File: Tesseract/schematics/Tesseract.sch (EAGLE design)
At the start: 108 parts, among them IC1 MC7805CDTG, IC2 QUAD_OPAMPD, IC3 NE5532D, IC4 LM4040B10, IC5 NE5532D, Q1 SI2309CDS, Q2 BSS123, Q901 BC846

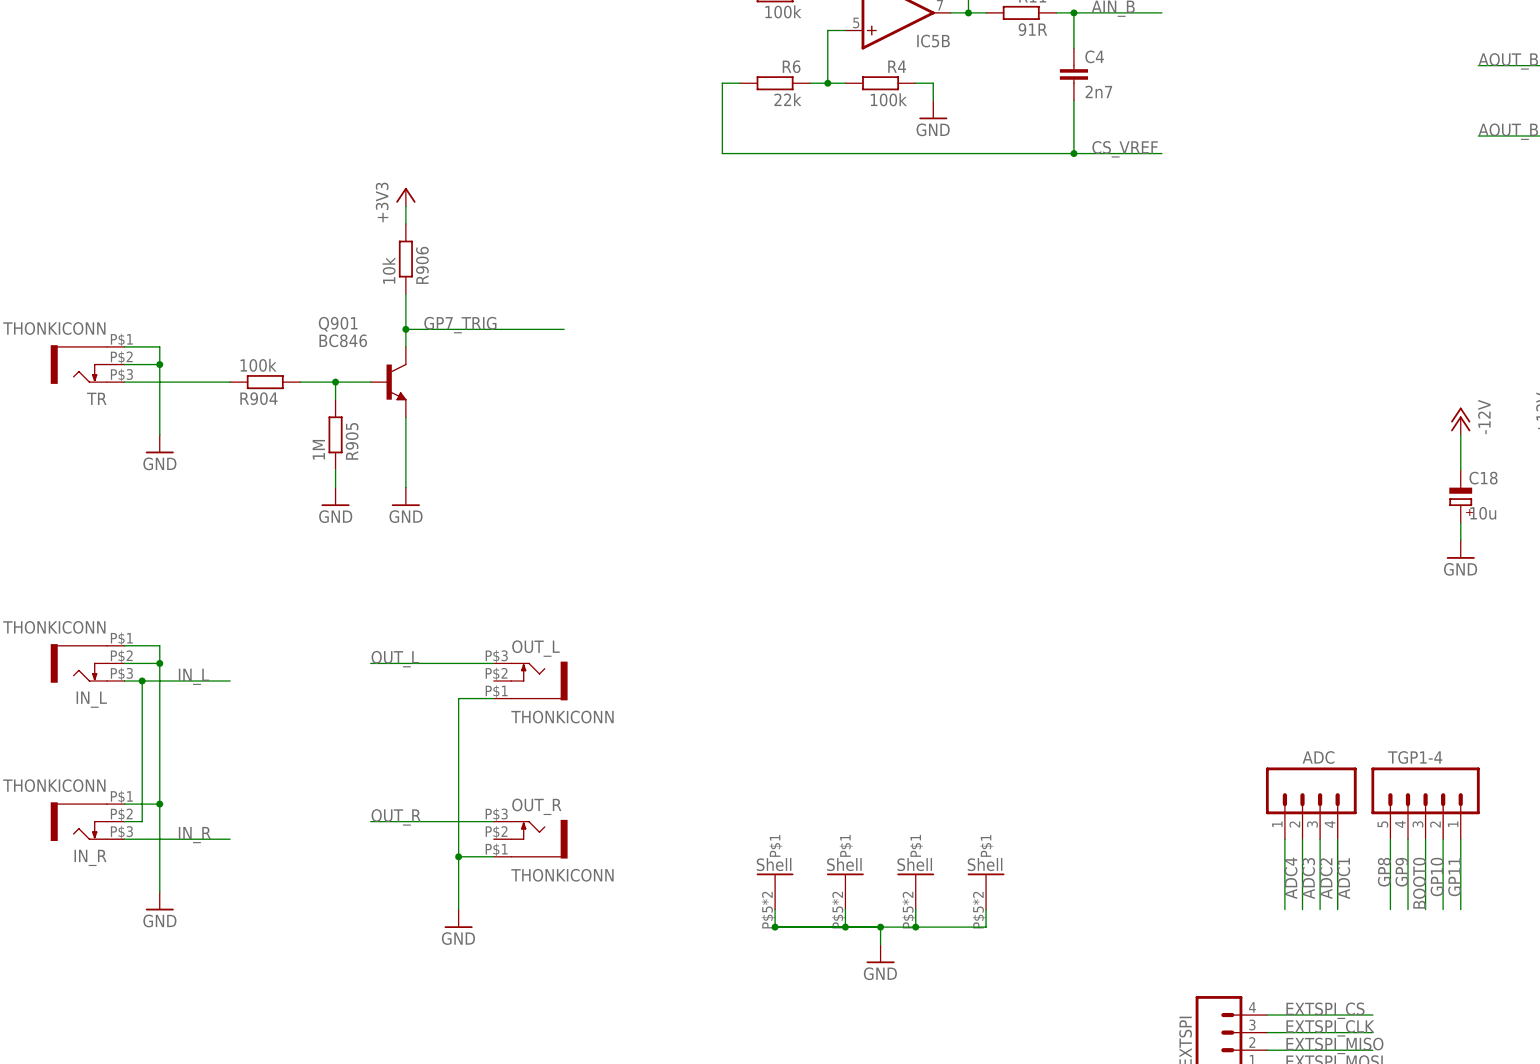
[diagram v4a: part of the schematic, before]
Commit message: added tempo out to normalled trigger input
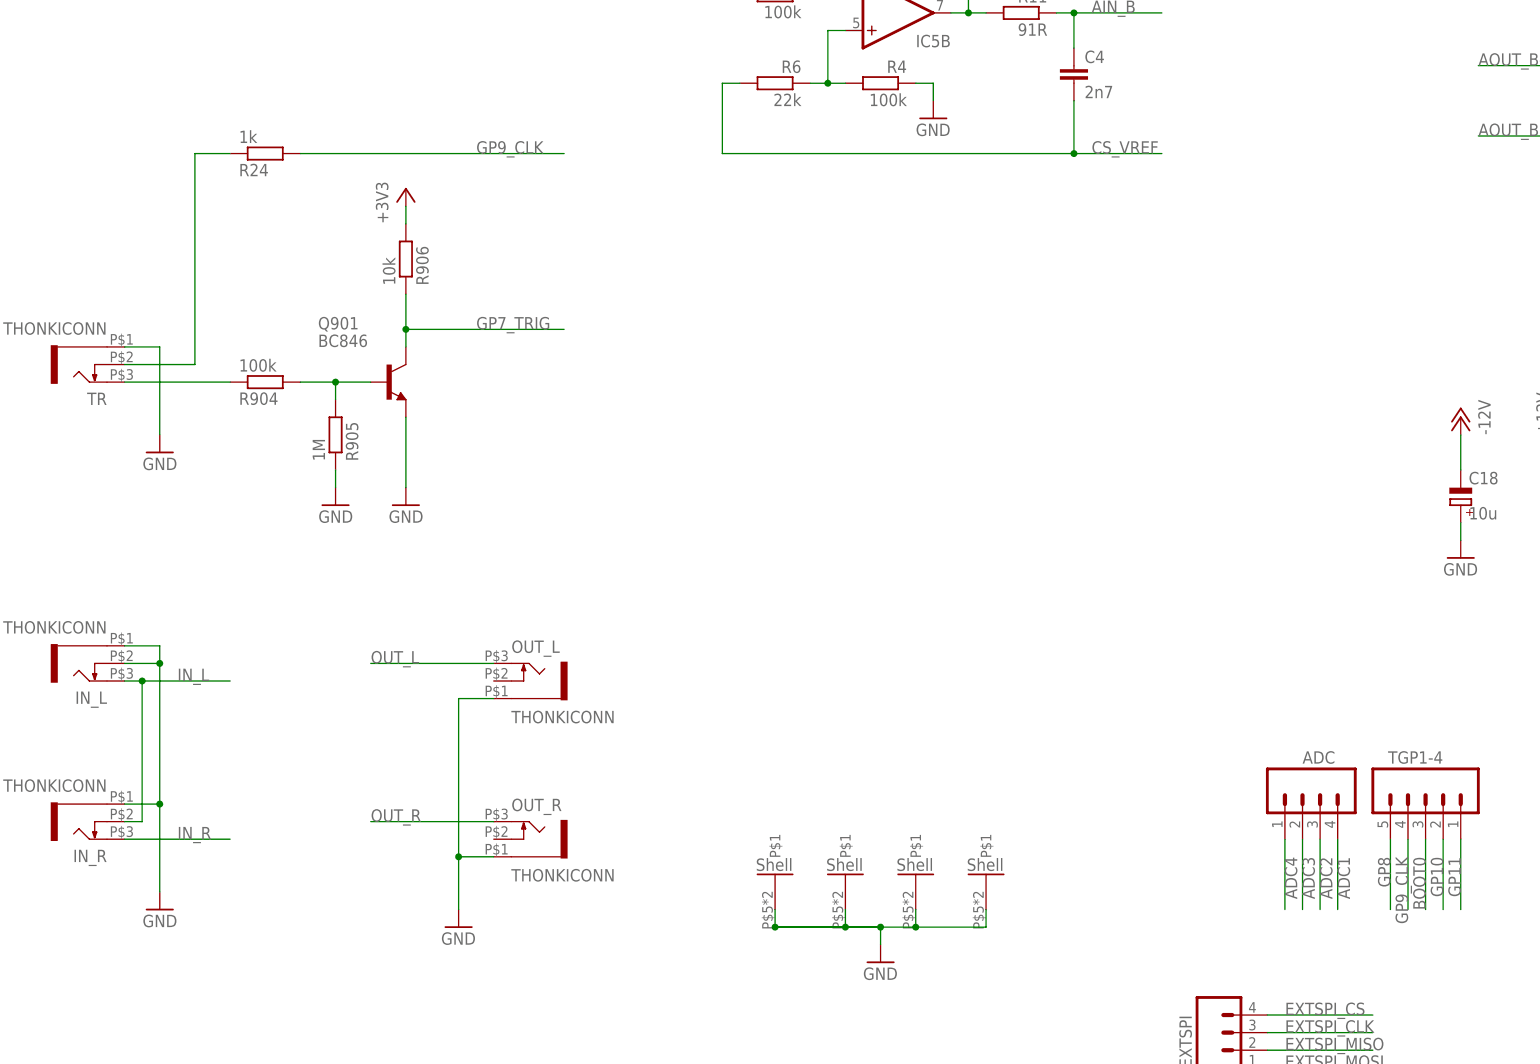
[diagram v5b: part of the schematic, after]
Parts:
- added R24: 1k, Rebel:R-EU_0603
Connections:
- removed net GP9: TGP1-4.4
- new net GP9_CLK: R24.2, TGP1-4.4
- new net N$38: R24.1, TR.4
- net GND: no longer TR.4
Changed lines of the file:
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@@
 <part name="C14" library="rcl" deviceset="CPOL-EU" device="C" value="47u"/>
 <part name="LED1" library="Rebel" deviceset="MULTICOMP_703-1028" device=""/>
+<part name="R24" library="Rebel" deviceset="R-EU_" device="0603" value="1k"/>
 </parts>
 <sheets>
@@
 <instance part="C14" gate="G$1" x="185.42" y="91.44"/>
 <instance part="LED1" gate="G$1" x="-58.42" y="198.12" rot="R90"/>
+<instance part="R24" gate="G$1" x="-40.64" y="139.7" rot="MR180"/>
 </instances>
 <busses>
@@
 </segment>
 <segment>
-<wire x1="-55.88" y1="111.76" x2="-55.88" y2="109.22" width="0.1524" layer="91"/>
 <pinref part="TR" gate="G$1" pin="5"/>
-<wire x1="-55.88" y1="109.22" x2="-55.88" y2="99.06" width="0.1524" layer="91"/>
+<wire x1="-55.88" y1="111.76" x2="-55.88" y2="99.06" width="0.1524" layer="91"/>
 <wire x1="-60.96" y1="111.76" x2="-55.88" y2="111.76" width="0.1524" layer="91"/>
 <pinref part="GND21" gate="1" pin="GND"/>
-<pinref part="TR" gate="G$1" pin="4"/>
-<wire x1="-60.96" y1="109.22" x2="-55.88" y2="109.22" width="0.1524" layer="91"/>
-<junction x="-55.88" y="109.22"/>
 </segment>
 <segment>
@@
 </segment>
 </net>
-<net name="GP9" class="0">
-<segment>
-<wire x1="124.46" y1="40.64" x2="124.46" y2="30.48" width="0.1524" layer="91"/>
-<label x="124.46" y="38.1" size="1.778" layer="95" rot="MR270"/>
-<pinref part="TGP1-4" gate="G$1" pin="4"/>
-</segment>
-</net>
 <net name="GP11" class="0">
 <segment>
@@
 <wire x1="-20.32" y1="114.3" x2="2.54" y2="114.3" width="0.1524" layer="91"/>
 <junction x="-20.32" y="114.3"/>
-<label x="-17.78" y="114.3" size="1.778" layer="95"/>
+<label x="-10.16" y="114.3" size="1.778" layer="95"/>
 <pinref part="Q901" gate="G$1" pin="C"/>
 </segment>
@@
 </segment>
 </net>
+<net name="N$38" class="0">
+<segment>
+<pinref part="TR" gate="G$1" pin="4"/>
+<wire x1="-60.96" y1="109.22" x2="-50.8" y2="109.22" width="0.1524" layer="91"/>
+<wire x1="-50.8" y1="109.22" x2="-50.8" y2="139.7" width="0.1524" layer="91"/>
+<pinref part="R24" gate="G$1" pin="1"/>
+<wire x1="-50.8" y1="139.7" x2="-45.72" y2="139.7" width="0.1524" layer="91"/>
+</segment>
+</net>
+<net name="GP9_CLK" class="0">
+<segment>
+<pinref part="R24" gate="G$1" pin="2"/>
+<wire x1="-35.56" y1="139.7" x2="2.54" y2="139.7" width="0.1524" layer="91"/>
+<label x="-10.16" y="139.7" size="1.778" layer="95"/>
+</segment>
+<segment>
+<wire x1="124.46" y1="40.64" x2="124.46" y2="30.48" width="0.1524" layer="91"/>
+<label x="124.46" y="38.1" size="1.778" layer="95" rot="MR270"/>
+<pinref part="TGP1-4" gate="G$1" pin="4"/>
+</segment>
+</net>

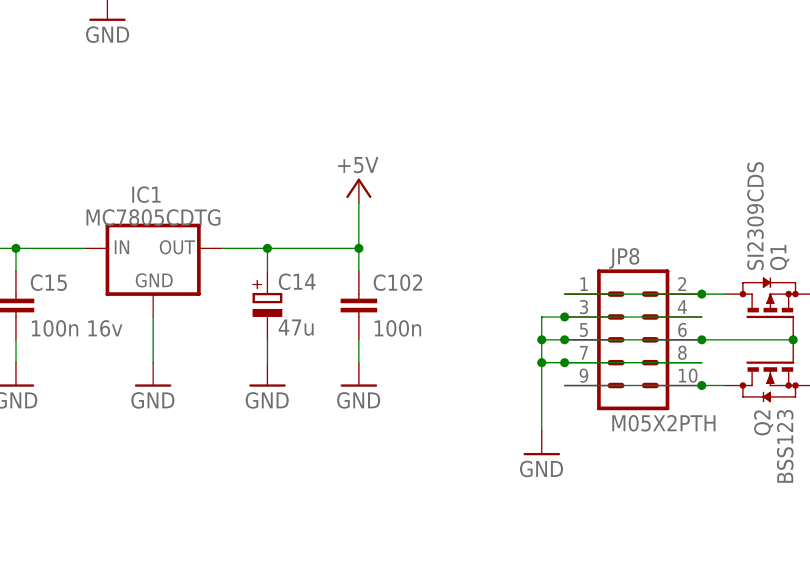
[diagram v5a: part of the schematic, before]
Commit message: renamed component
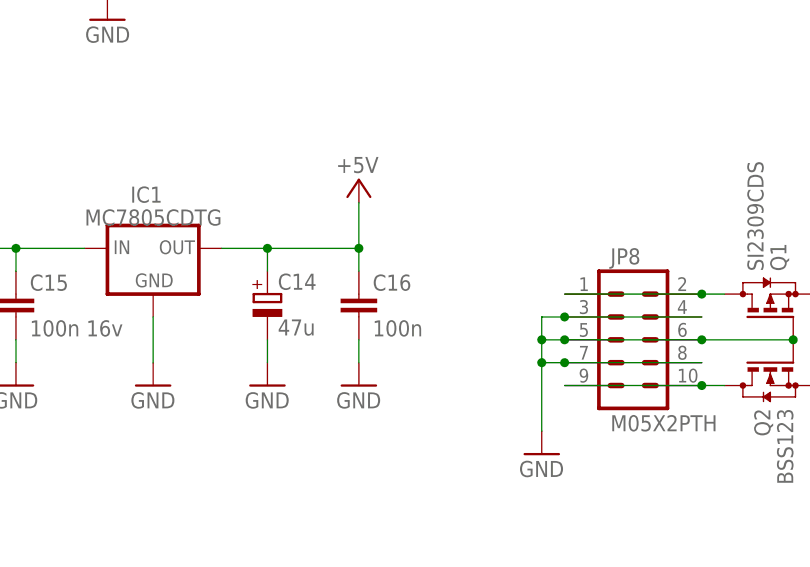
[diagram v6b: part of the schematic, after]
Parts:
- renumbered C102 to C16
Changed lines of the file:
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@@
 <attribute name="OC_FARNELL" value="1843725"/>
 </part>
-<part name="C102" library="Rebel" deviceset="C-EU" device="C0603" value="100n"/>
+<part name="C16" library="Rebel" deviceset="C-EU" device="C0603" value="100n"/>
 <part name="C15" library="Rebel" deviceset="C-EU" device="C0603" value="100n 16v"/>
 <part name="GND31" library="supply1" deviceset="GND" device=""/>
@@
 <attribute name="OC_FARNELL" x="241.3" y="81.28" size="1.778" layer="96" rot="MR270" display="off"/>
 </instance>
-<instance part="C102" gate="G$1" x="195.58" y="91.44"/>
+<instance part="C16" gate="G$1" x="195.58" y="91.44"/>
 <instance part="C15" gate="G$1" x="157.48" y="91.44"/>
 <instance part="GND31" gate="1" x="157.48" y="81.28"/>
@@
 </segment>
 <segment>
-<pinref part="C102" gate="G$1" pin="2"/>
+<pinref part="C16" gate="G$1" pin="2"/>
 <pinref part="GND59" gate="1" pin="GND"/>
 <wire x1="195.58" y1="83.82" x2="195.58" y2="86.36" width="0.1524" layer="91"/>
@@
 </segment>
 <segment>
-<pinref part="C102" gate="G$1" pin="1"/>
+<pinref part="C16" gate="G$1" pin="1"/>
 <wire x1="195.58" y1="93.98" x2="195.58" y2="96.52" width="0.1524" layer="91"/>
 <wire x1="180.34" y1="96.52" x2="185.42" y2="96.52" width="0.1524" layer="91"/>

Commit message: renumbered components and slimmed board
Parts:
- removed C500: 100n, resistor:C-EUC0603
- removed R300, R500, R501: 100k, Rebel:R-EU_0603
- removed R400, R402: 5k6, Rebel:R-EU_0603
- removed R404: 10k, Rebel:R-EU_0603
- removed R406: 1k, Rebel:R-EU_0603
- removed R503, R603: 33k, Rebel:R-EU_0603
- added C19: 100n, resistor:C-EUC0603
- added R25: 4k7, Rebel:R-EU_0603
- added R26: 5k6, Rebel:R-EU_0603
- added R27, R36: 1k, Rebel:R-EU_0603
- added R28: 10k, Rebel:R-EU_0603
- added R29: 150R, Rebel:R-EU_0603
- added R43, R44, R45: 510R, Rebel:R-EU_0603
- C1: value 100n -> 100n 16v; device resistor:C-EUC0603 -> Rebel:C-EUC0603
- C11: value 1n -> 100p
- C13: value 100n -> 1n
- C14: value 47u -> 1n; device rcl:CPOL-EUC -> resistor:C-EUC0603
- C15: value 100n 16v -> 100n; device Rebel:C-EUC0603 -> resistor:C-EUC0603
- C16: value 100n -> 100p; device Rebel:C-EUC0603 -> resistor:C-EUC0603
- C17: value 10u -> 100n; device Rebel:CPOL-EU153CLV-0505 -> resistor:C-EUC0603
- C18: value 10u -> 1n; device Rebel:CPOL-EU153CLV-0505 -> resistor:C-EUC0603
- C2: value 100n -> 10u; device resistor:C-EUC0603 -> Rebel:CPOL-EU153CLV-0505
- C3: value 2n7 -> 100n; device resistor:C-EUC0603 -> Rebel:C-EUC0603
- C4: value 2n7 -> 10u; device resistor:C-EUC0603 -> Rebel:CPOL-EU153CLV-0505
- C5: value 100n -> 47u; device resistor:C-EUC0603 -> rcl:CPOL-EUC
- C6, C9: value 100p -> 100n
- C7, C8: value 1n -> 2n7
- IC2: value QUAD_OPAMPD -> NE5532D; device adafruit:QUAD_OPAMPD -> linear:NE5532D
- IC4: value LM4040B10 -> QUAD_OPAMPD; device texas:LM4041C12DBZ -> adafruit:QUAD_OPAMPD
- IC5: value NE5532D -> LM4040B10; device linear:NE5532D -> texas:LM4041C12DBZ
- Q1: value SI2309CDS -> BSS123; device transistor-small-signal:BSS84 -> transistor-small-signal:BSS123; OC_FARNELL 1779264 -> 1843725
- Q2: value BSS123 -> SI2309CDS; device transistor-small-signal:BSS123 -> transistor-small-signal:BSS84; OC_FARNELL 1843725 -> 1779264
- R1: value 4k7 -> 22k
- R11: value 91R -> 22k
- R12: value 10k -> 100k
- R13: value 100k -> 1k
- R14: value 1k -> 10k
- R15: value 150R -> 4k7
- R17: value 5k6 -> 10k
- R19: value 4k7 -> 5k6
- R2: value 4k7 -> 100k
- R20: value 10k -> 4k7
- R21: value 510R -> 10k
- R22: value 510R -> 5k6
- R23: value 510R -> 33k
- R24: value 1k -> 33k
- R3, R8, R9: value 22k -> 100k
- R4: value 100k -> 22k
- R7: value 10k -> 91R
- renumbered C501 to C20, D500 to D1, D600 to D2, D700 to D3, D800 to D4, Q901 to Q3, R504 to R40, R505 to R39, R600 to R32, R601 to R31, R604 to R42, R605 to R41, R700 to R30, R701 to R33, R703 to R35, R704 to R47, R705 to R46, R800 to R38, R801 to R37, R803 to R34, R804 to R52, R805 to R51, R904 to R50, R905 to R49, R906 to R48
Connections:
- net +12V: now also C1.1, C17.1, C4.+, C9.1, IC4P.V+, Q2.S; no longer C12.1, C17.+, C2.1, C500.1, IC5P.V+, Q1.S
- net +5V: now also C3.1, C5.+; no longer C14.+, C16.1
- net -12V: now also C12.2, C2.-, C6.2, IC4P.V-, Q1.S, R29.1; no longer C13.2, C18.-, C5.2, IC5P.V-, Q2.S, R15.1
- net AIN_A: now also C7.1, R7.1; no longer C3.1, R10.1
- net AIN_B: now also C8.1, R10.1; no longer C4.1, R11.1
- net AOUT_A+: now also R19.1; no longer R402.1
- net AOUT_A-: now also R16.1; no longer R400.1
- net AOUT_B+: now also R22.1; no longer R17.1
- net AOUT_B-: now also R26.1; no longer R16.1
- net CS_VREF: now also C7.2, C8.2, R4.2; no longer C3.2, C4.2, R8.2
- net CV_REF: now also C19.1, IC5.A, R29.2; no longer C1.1, IC4.A, R15.2
- net GND: now also C12.1, C13.2, C14.2, C17.2, C18.2, C19.2, C2.+, C3.2, C4.-, C5.-, C6.1, C9.2, IC4A.+IN, IC4B.+IN, IC4C.+IN, IC4D.+IN, IC5.C, R17.1, R21.1, R3.1; no longer C11.2, C12.2, C13.1, C14.-, C16.2, C17.-, C18.+, C2.2, C5.1, C500.2, C7.2, C8.2, IC2A.+IN, IC2B.+IN, IC2C.+IN, IC2D.+IN, IC4.C, R20.1, R4.1, R7.1
- net GP1_LEDPWM: now also R43.2; no longer R23.2
- net GP2_LEDPWM: now also R44.2; no longer R22.2
- net GP6_LEDPWM: now also R45.2; no longer R21.2
- net GP9_CLK: now also R36.2; no longer R24.2
- net IN_L: now also R2.2; no longer R300.2
- net IN_R: now also R12.2; no longer R13.2
- net N$1: now also IC2A.OUT, R1.1, R7.2; no longer IC5A.OUT, R10.2, R3.1
- net N$10: now also IC2B.OUT, R10.2, R11.1; no longer IC5B.OUT, R11.2, R9.1
- net N$11: now also R18.2; no longer R2.2
- net N$12: now also Q2.D; no longer Q1.D
- net N$13: now also IC4A.-IN, R23.1, R8.2, R9.2; no longer IC2A.-IN, R500.2, R501.2, R503.1
- net N$14: now also R9.1; no longer R500.1
- net N$15: now also C13.1, R17.2, R18.1, R19.2; no longer C7.1, R2.1, R402.2, R7.2
- net N$17: now also IC4A.OUT, R23.2; no longer IC2A.OUT, R503.2
- net N$18: now also C16.2, R27.1, R28.2; no longer C9.2, R12.2, R14.1
- net N$2: now also IC2A.+IN, R3.2, R4.1; no longer IC5A.+IN, R5.2, R8.1
- net N$20: now also IC4B.-IN, R24.1; no longer IC2B.-IN, R603.1
- net N$22: now also IC4B.OUT, R24.2; no longer IC2B.OUT, R603.2
- net N$24: now also C18.1, R25.1, R26.2, R28.1; no longer C11.1, R12.1, R16.2, R18.1
- net N$26: now also C16.1, R25.2; no longer C9.1, R18.2
- net N$28: now also IC4C.OUT; no longer IC2C.OUT
- net N$3: now also R8.1; no longer R501.1
- net N$30: now also R20.2; no longer R19.2
- net N$32: now also C14.1, R20.1, R21.2, R22.2; no longer C10.1, R17.2, R19.1, R20.2
- net N$33: now also IC4D.-IN; no longer IC2D.-IN
- net N$35: now also IC4D.OUT; no longer IC2D.OUT
- net N$38: now also R36.1; no longer R24.1
- net N$39: now also C11.2, R13.1, R14.2; no longer C6.2, R404.2, R406.1
- net N$4: now also IC2B.+IN, R5.2; no longer IC5B.+IN, R4.2
- net N$40: now also R43.1; no longer R23.1
- net N$41: now also C10.1, R14.1, R15.1, R16.2; no longer C8.1, R1.1, R400.2, R404.1
- net N$42: now also R45.1; no longer R21.1
- net N$43: now also R44.1; no longer R22.1
- net N$5: now also IC2B.-IN, R11.2, R12.1; no longer IC5B.-IN, R13.1, R9.2
- net N$6: now also IC4C.-IN; no longer IC2C.-IN
- net N$7: now also C11.1, R15.2; no longer C6.1, R1.2
- net N$8: now also Q1.D; no longer Q2.D
- net N$9: now also IC2A.-IN, R1.2, R2.1; no longer IC5A.-IN, R3.2, R300.1
- net OUT_L: now also R13.2; no longer R406.2
- net OUT_R: now also R27.2; no longer R14.2
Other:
- moved on the sheet: C1, C10, C11, C12, C13, C15, C16, C3, C6, C7, C8, C9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
